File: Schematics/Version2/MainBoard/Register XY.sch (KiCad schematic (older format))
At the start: 13 parts, among them J11 XY LED Connector, U10 74F161, U11 74F161, U6 74F161, U7 74LS245, U8 74F161, U9 74LS245

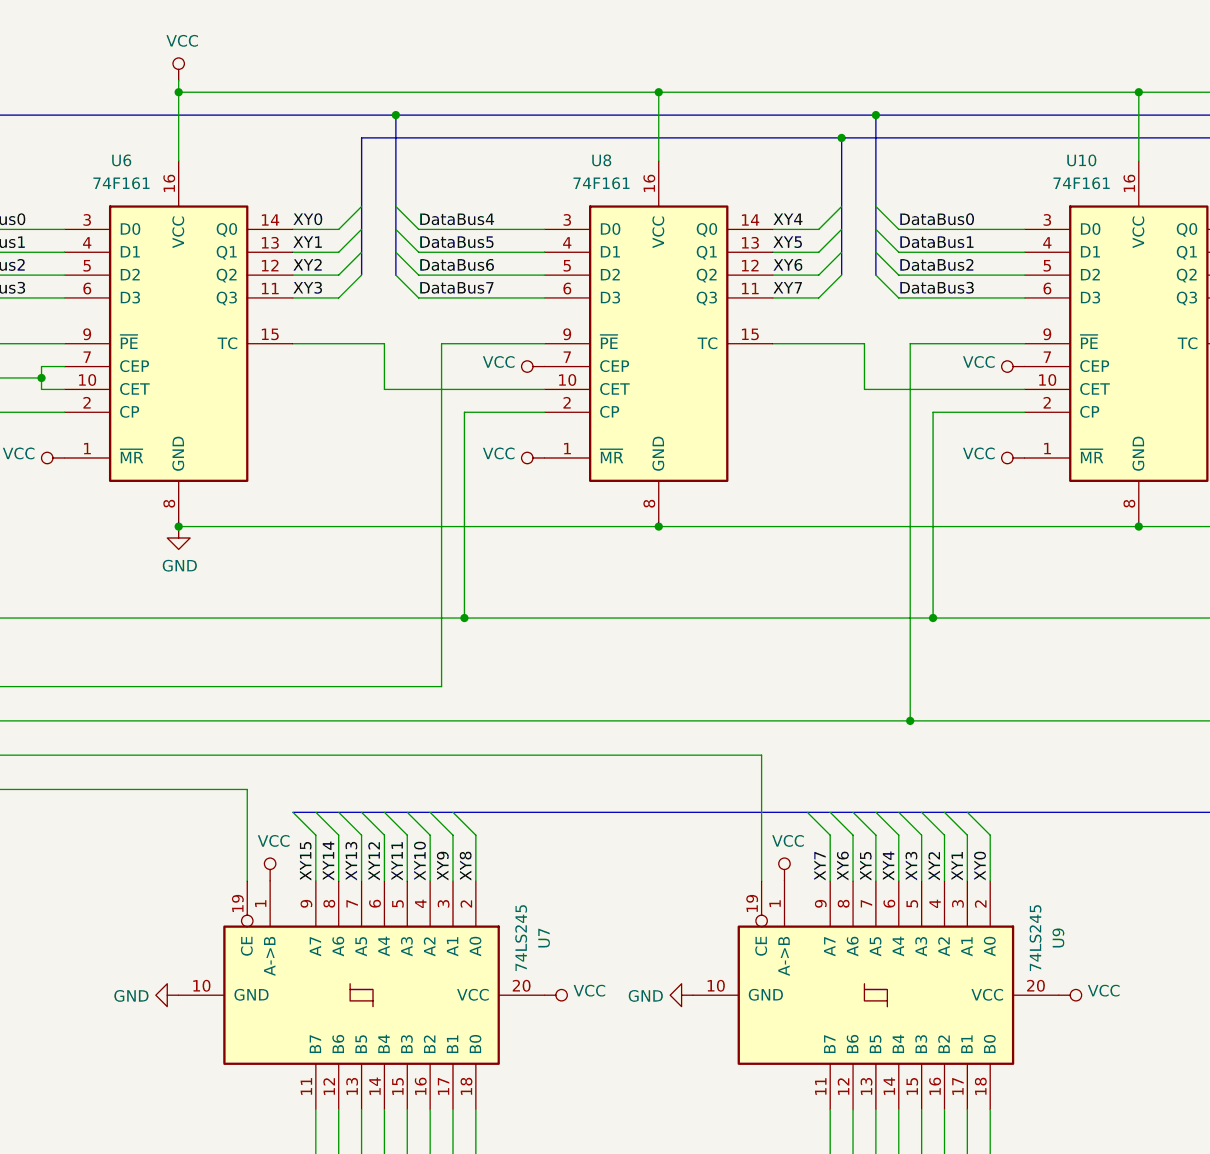
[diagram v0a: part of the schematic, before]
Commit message: Merge branch "version2a"
This replaces the Version2 schematics with a new second version. This one
completes a four layer routing of the main board.
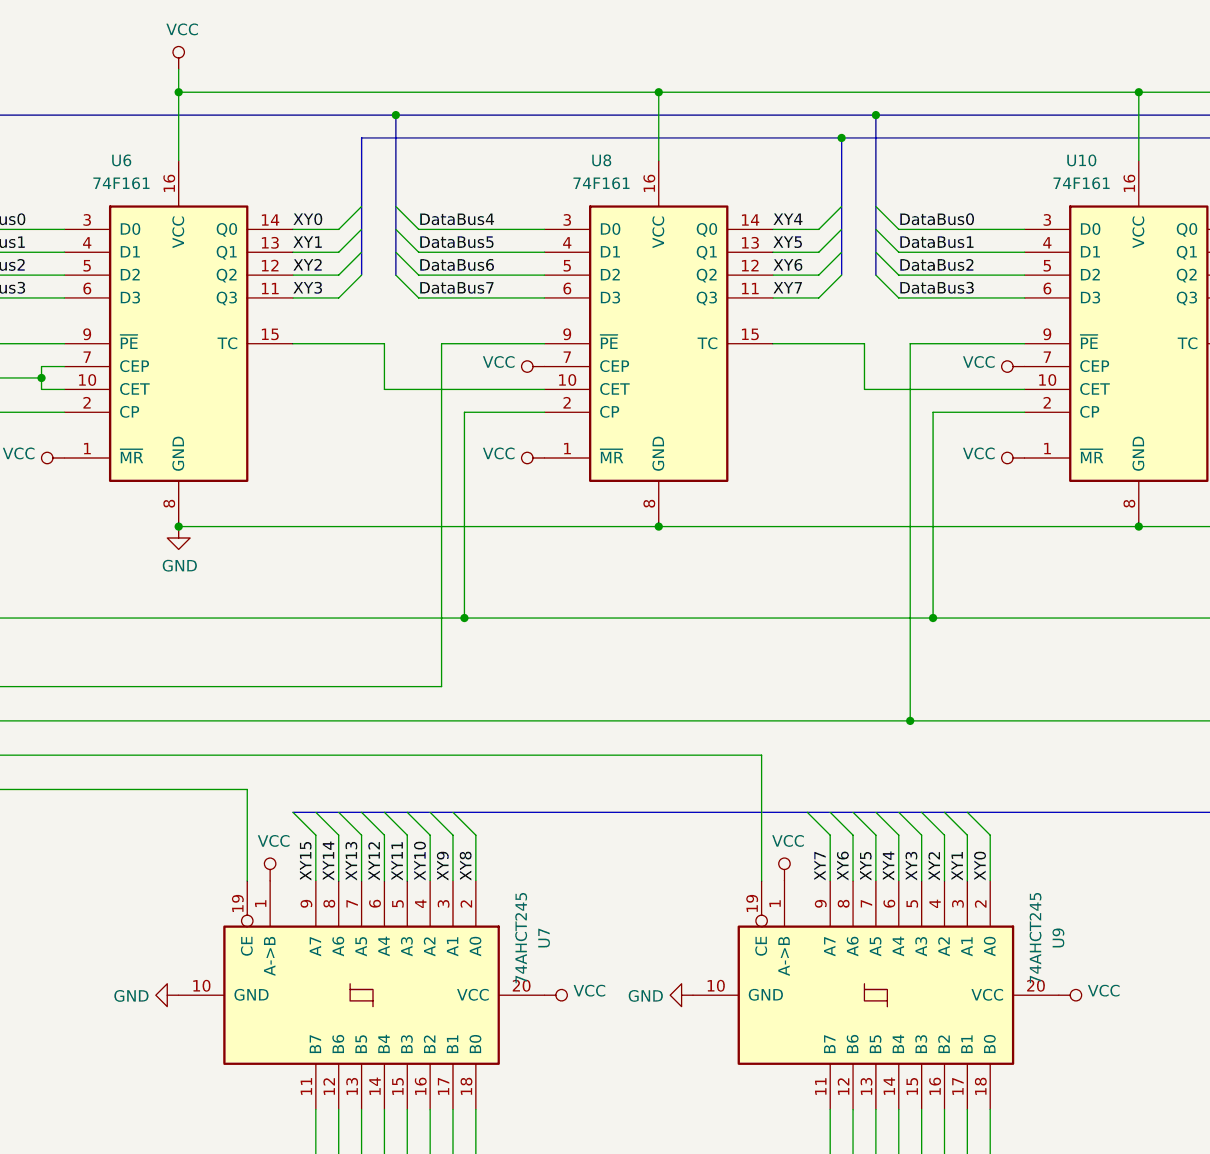
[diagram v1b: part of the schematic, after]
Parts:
- U7, U9: value 74LS245 -> 74AHCT245
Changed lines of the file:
@@
 $Descr USLetter 11000 8500
 encoding utf-8
-Sheet 3 22
+Sheet 3 23
 Title "Registers X and Y"
 Date ""
@@
 Wire Wire Line
 	2450 1300 2450 1000
-Connection ~ 2450 1000
-Wire Wire Line
-	2450 950  2450 1000
-$Comp
-L power:VCC #PWR?
-U 1 1 5DBCA97A
-P 2450 950
-AR Path="/5D2C07CD/5DBCA97A" Ref="#PWR?"  Part="1"
-AR Path="/5D7BD0EA/5DBCA97A" Ref="#PWR0256"  Part="1"
-F 0 "#PWR0256" H 2450 800 50  0001 C CNN
-F 1 "VCC" H 2467 1123 50  0000 C CNN
-F 2 "" H 2450 950 50  0001 C CNN
-F 3 "" H 2450 950 50  0001 C CNN
-	1    2450 950
-	1    0    0    -1
-$EndComp
 Text Label 3500 1700 0    50   ~ 0
 DataBus5
@@
 AR Path="/5D7BD0EA/5DDC9F0A" Ref="U7"  Part="1"
 F 0 "U7" H 3000 5750 50  0000 C CNN
-F 1 "74LS245" H 3000 5650 50  0000 C CNN
+F 1 "74AHCT245" H 3000 5650 50  0000 C CNN
 F 2 "Package_DIP:DIP-20_W7.62mm" H 3250 4950 50  0001 C CNN
-F 3 "http://www.ti.com/lit/gpn/sn74LS245" H 3250 4950 50  0001 C CNN
+F 3 "http://www.ti.com/lit/ds/symlink/sn54ahct245.pdf" H 3250 4950 50  0001 C CNN
 	1    3250 4950
 	0    1    1    0
@@
 AR Path="/5D7BD0EA/5DDD930F" Ref="U9"  Part="1"
 F 0 "U9" H 5250 5750 50  0000 C CNN
-F 1 "74LS245" H 5250 5650 50  0000 C CNN
+F 1 "74AHCT245" H 5250 5650 50  0000 C CNN
 F 2 "Package_DIP:DIP-20_W7.62mm" H 5500 4950 50  0001 C CNN
-F 3 "http://www.ti.com/lit/gpn/sn74LS245" H 5500 4950 50  0001 C CNN
+F 3 "http://www.ti.com/lit/ds/symlink/sn54ahct245.pdf" H 5500 4950 50  0001 C CNN
 	1    5500 4950
 	0    1    1    0
@@
 	1    0    0    -1
 $EndComp
-Wire Bus Line
-	3150 6500 9900 6500
-Wire Bus Line
-	2950 4150 9600 4150
-Wire Bus Line
-	9600 1200 9600 4150
-Wire Bus Line
-	7450 1200 7450 1800
-Wire Bus Line
-	5350 1200 5350 1800
-Wire Bus Line
-	3250 1200 3250 1800
-Wire Bus Line
-	7600 1100 7600 1800
-Wire Bus Line
-	5500 1100 5500 1800
-Wire Bus Line
-	3400 1100 3400 1800
-Wire Bus Line
-	1350 1100 1350 1800
 Text GLabel 1400 6550 0    50   Input ~ 0
 XY[0..15]
@@
 Wire Bus Line
 	1650 6550 1400 6550
+$Comp
+L power:VCC #PWR0240
+U 1 1 5E1BD4C2
+P 2450 900
+F 0 "#PWR0240" H 2450 750 50  0001 C CNN
+F 1 "VCC" H 2467 1073 50  0000 C CNN
+F 2 "" H 2450 900 50  0001 C CNN
+F 3 "" H 2450 900 50  0001 C CNN
+	1    2450 900
+	1    0    0    -1
+$EndComp
+Wire Wire Line
+	2450 900  2450 1000
+Connection ~ 2450 1000
+Wire Bus Line
+	9600 1200 9600 4150
+Wire Bus Line
+	7450 1200 7450 1800
+Wire Bus Line
+	5350 1200 5350 1800
+Wire Bus Line
+	3250 1200 3250 1800
+Wire Bus Line
+	7600 1100 7600 1800
+Wire Bus Line
+	5500 1100 5500 1800
+Wire Bus Line
+	3400 1100 3400 1800
+Wire Bus Line
+	1350 1100 1350 1800
+Wire Bus Line
+	3150 6500 9900 6500
+Wire Bus Line
+	2950 4150 9600 4150
 $EndSCHEMATC

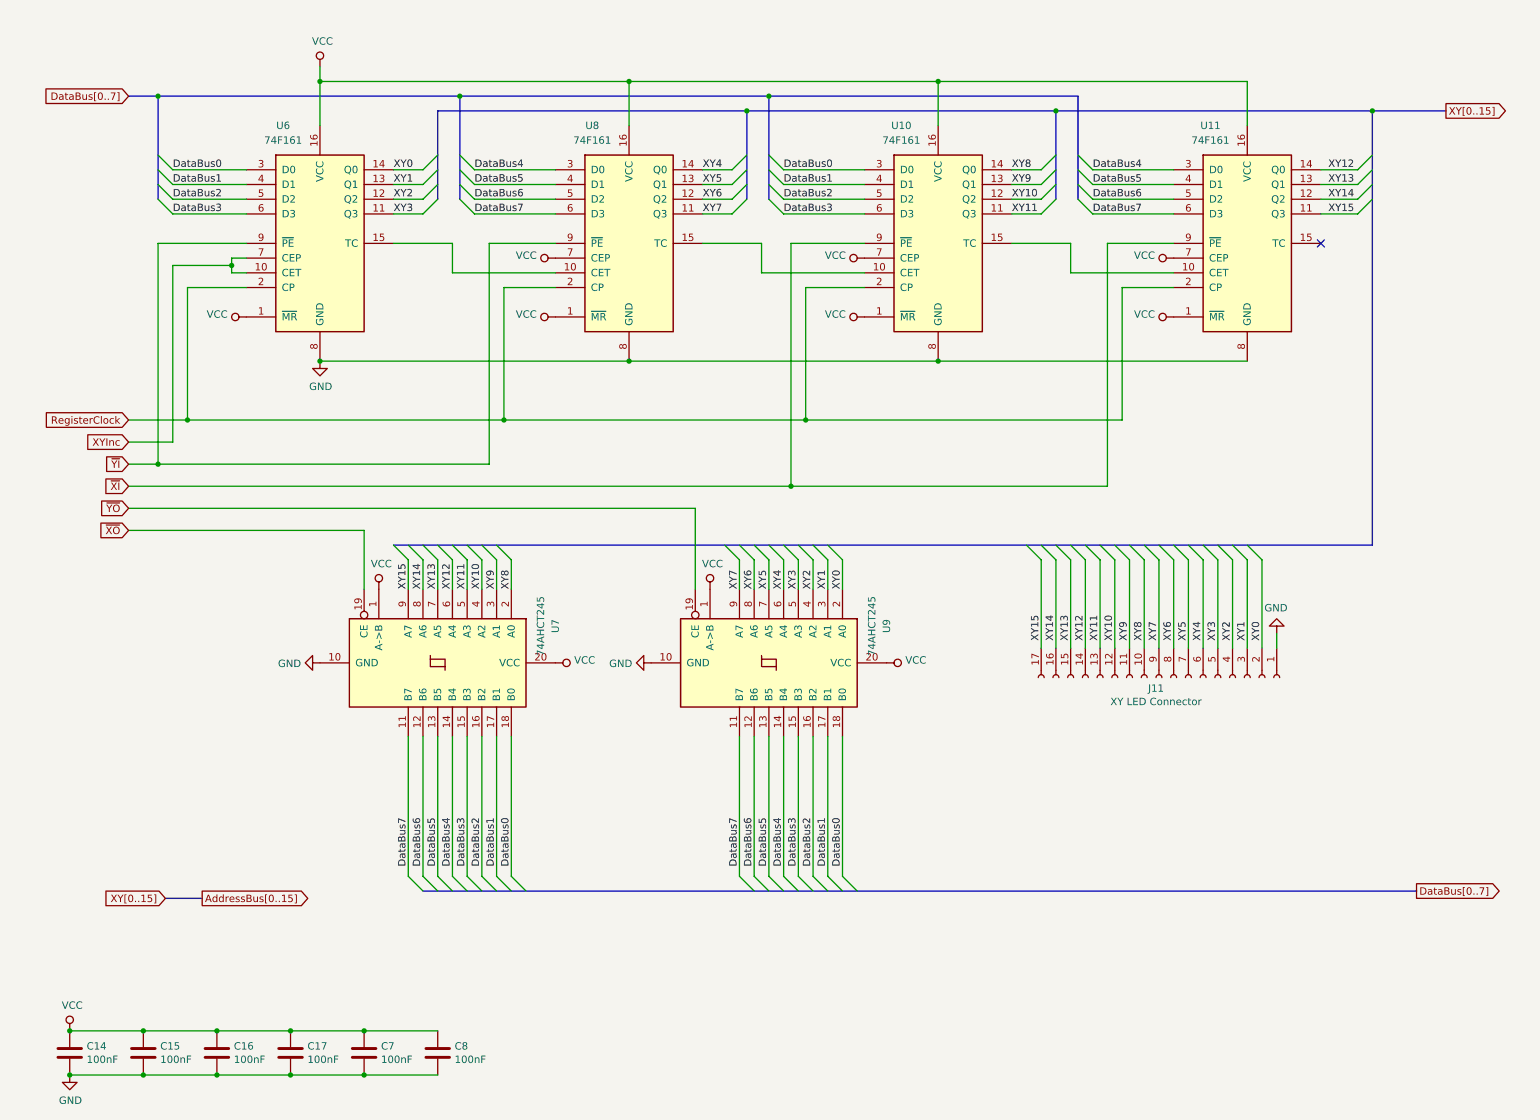
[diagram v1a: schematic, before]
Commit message: Merge branch "version2b".
This is a new version of the computer which incorporates a number of
improvements:
  * Uses a four layer PCB instead of six.
  * Replaced the clock with a new circuit. This is simpler, but allows for
    an external clock to be attached.
  * Changes to the ALU to have it operate over two clock cycles instead of
    one. This fixes a timing issue which makes the ALU unreliable at 10MHz.
  * Replaced instruction RAM with dual port SRAM.
  * Replaced the physical connector for expansion cards to interleave
    signals with ground.
  * Added places where components can be attached to provide AC termination
    of the data bus, should this be necessary.
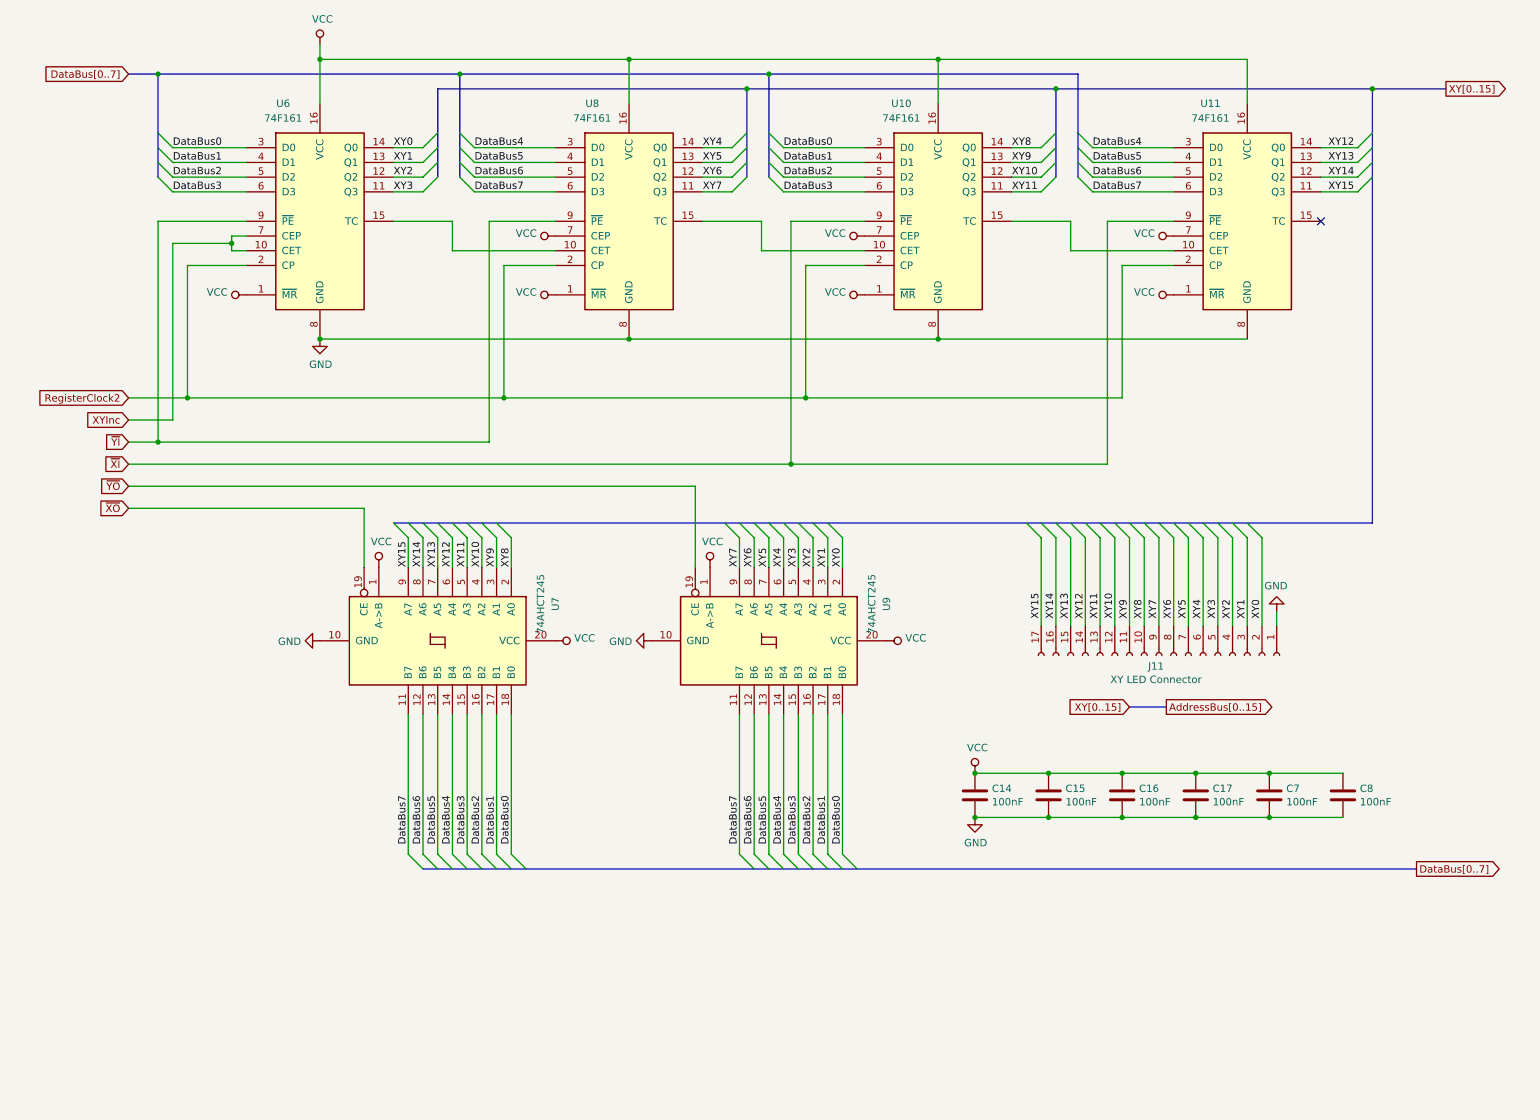
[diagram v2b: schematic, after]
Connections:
- net RegisterClock renamed RegisterClock2
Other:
- moved on the sheet: C14, C15, C16, C17, C7, C8, J11, U10, U11, U6, U7, U8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
